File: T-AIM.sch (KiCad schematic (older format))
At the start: 30 parts, among them IC1 ATMEGA328PB-A

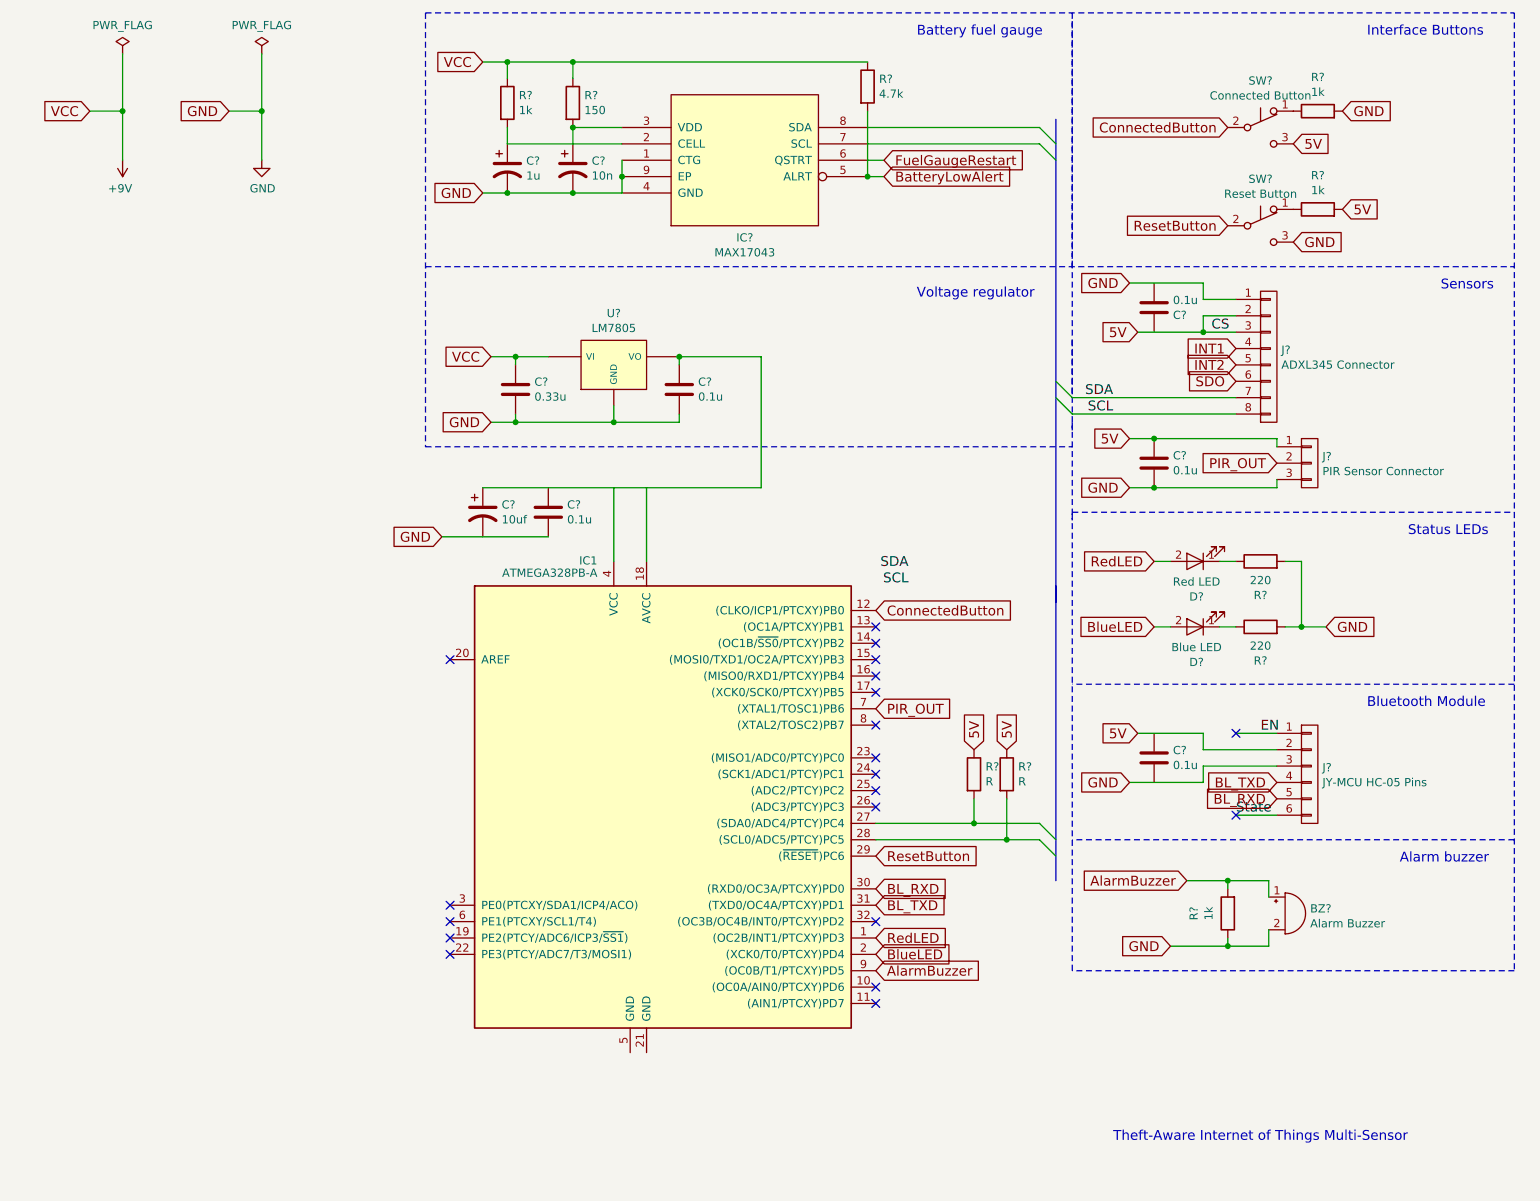
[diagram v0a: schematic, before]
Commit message: Schematic switches changed; PCB footprints assigned; Preliminary PCB layout set
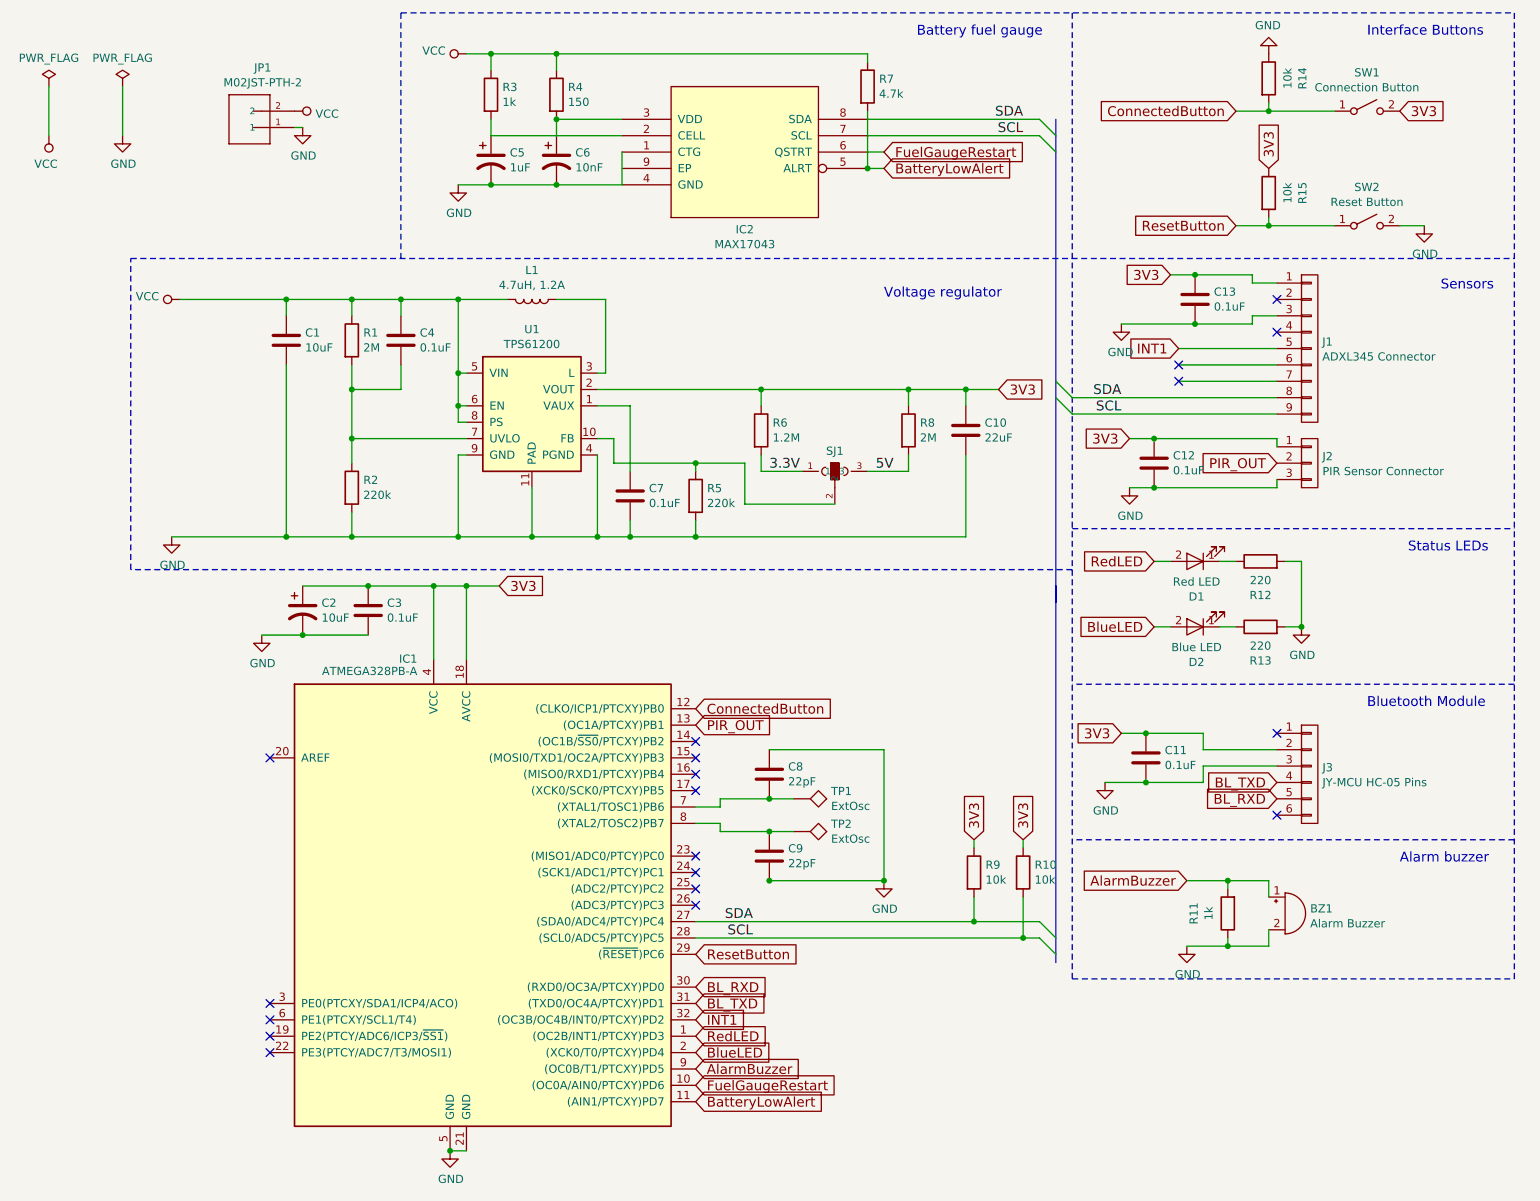
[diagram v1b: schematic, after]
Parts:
- removed BZ?: Alarm Buzzer, symbol Buzzer
- removed C? (x5): 0.1u, symbol C
- removed C?: 0.33u, symbol C
- removed C?: 1u, symbol CP1
- removed C?: 10n, symbol CP1
- removed C?: 10uf, symbol CP1
- removed D?: Red LED, symbol LED
- removed D?: Blue LED, symbol LED
- removed IC?: MAX17043, symbol MAX17043
- removed J?: ADXL345 Connector, symbol CONN_01X08
- removed J?: PIR Sensor Connector, symbol CONN_01X03
- removed J?: JY-MCU HC-05 Pins, symbol CONN_01X06
- removed R? (x2): 220, symbol R
- removed R? (x4): 1k, symbol R
- removed R? (x2): R, symbol R
- removed R?: 4.7k, symbol R
- removed R?: 150, symbol R
- removed SW?: Reset Button, symbol SW_Push_SPDT
- removed SW?: Connected Button, symbol SW_Push_SPDT
- removed U?: LM7805, symbol LM7805
- added BZ1: Alarm Buzzer, T-AIM:AT-1220-TT-9-R, symbol Buzzer
- added C1: 10uF, Capacitors_SMD:C_1812_HandSoldering, symbol C
- added C10: 22uF, Capacitors_SMD:C_1812_HandSoldering, symbol C
- added C11, C12, C13, C3, C4, C7: 0.1uF, Capacitors_SMD:C_1812_HandSoldering, symbol C
- added C2: 10uF, Capacitors_SMD:CP_Elec_5x5.3, symbol CP1
- added C5: 1uF, Capacitors_SMD:CP_Elec_5x5.3, symbol CP1
- added C6: 10nF, Capacitors_SMD:CP_Elec_5x5.3, symbol CP1
- added C8, C9: 22pF, Capacitors_SMD:C_1812_HandSoldering, symbol C
- added D1: Red LED, SparkFun-LED:LED-1206, symbol LED
- added D2: Blue LED, SparkFun-LED:LED-1206, symbol LED
- added IC2: MAX17043, SparkFun-PowerIC:TDFN-8, symbol MAX17043
- added J1: ADXL345 Connector, Pin_Headers:Pin_Header_Straight_1x09_Pitch2.54mm, symbol CONN_01X09
- added J2: PIR Sensor Connector, TO_SOT_Packages_THT:TO-5-3, symbol CONN_01X03
- added J3: JY-MCU HC-05 Pins, Pin_Headers:Pin_Header_Straight_1x06_Pitch2.54mm, symbol CONN_01X06
- added JP1: M02JST-PTH-2, SparkFun-Connectors:JST-2-PTH, symbol M02JST-PTH-2
- added L1: 4.7uH, 1.2A, SparkFun-Passives:INDUCTOR_4.7UH, symbol L
- added R1, R8: 2M, Resistors_SMD:R_0805_HandSoldering, symbol R
- added R10, R14, R15, R9: 10k, Resistors_SMD:R_0805_HandSoldering, symbol R
- added R11, R3: 1k, Resistors_SMD:R_0805_HandSoldering, symbol R
- added R12, R13: 220, Resistors_SMD:R_0805_HandSoldering, symbol R
- added R2, R5: 220k, Resistors_SMD:R_0805_HandSoldering, symbol R
- added R4: 150, Resistors_SMD:R_0805_HandSoldering, symbol R
- added R6: 1.2M, Resistors_SMD:R_0805_HandSoldering, symbol R
- added R7: 4.7k, Resistors_SMD:R_0805_HandSoldering, symbol R
- added SJ1: SOLDERJUMPER_2WAY-OLDPASTE1&2, SparkFun-Passives:SJ_3, symbol SOLDERJUMPER_2WAY-OLDPASTE1&2
- added SW1: Connection Button, Buttons_Switches_SMD:SW_SPST_PTS645, symbol SW_SPST
- added SW2: Reset Button, Buttons_Switches_SMD:SW_SPST_PTS645, symbol SW_SPST
- added TP1, TP2: ExtOsc, Connectors:PINTST, symbol TEST
- added U1: TPS61200, SparkFun-PowerIC:DRC-10, symbol TPS61200
- IC1: footprint Housings_QFP:LQFP-32_5x5mm_Pitch0.5mm -> Housings_QFP:TQFP-32_7x7mm_Pitch0.8mm
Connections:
- net 5V: now also R8.2, SJ1.3
- net AlarmBuzzer: now also BZ1.1 (-), R11.2
- net BL_RXD: now also J3.5 (P5)
- net BL_TXD: now also J3.4 (P4)
- net BatteryLowAlert: now also IC1.11 ((AIN1/PTCXY)PD7), IC2.5 (ALRT), R7.2
- net BlueLED: now also D2.2 (A)
- net ConnectedButton: now also R14.2, SW1.1 (A)
- net FuelGaugeRestart: now also IC1.10 ((OC0A/AIN0/PTCXY)PD6), IC2.6 (QSTRT)
- net GND: now also IC1.21 (GND), IC1.5 (GND), BZ1.2 (+), C1.2, C10.2, C11.2, C12.2, C13.2, C2.2, C3.2, C5.2, C6.2, C7.2, C8.1, C9.2, IC2.1 (CTG), IC2.4 (GND), IC2.9 (EP), J1.3 (P3), J2.3 (P3), J3.3 (P3), JP1.1, R11.1, R12.2, R13.2, R14.1, R2.2, R5.2, SW2.2 (B), U1.11 (PAD), U1.4 (PGND), U1.9 (GND)
- net INT1: now also IC1.32 ((OC3B/OC4B/INT0/PTCXY)PD2), J1.5 (P5)
- net PIR_OUT: now also IC1.13 ((OC1A/PTCXY)PB1), J2.2 (P2); no longer IC1.7 ((XTAL1/TOSC1)PB6)
- net RedLED: now also D1.2 (A)
- net ResetButton: now also R15.2, SW2.1 (A)
- net SCL: now also IC1.28 ((SCL0/ADC5/PTCY)PC5), IC2.7 (SCL), J1.9 (P9), R10.2
- net SDA: now also IC1.27 ((SDA0/ADC4/PTCY)PC4), IC2.8 (SDA), J1.8 (P8), R9.2
- net 3V3: now reaches IC1.18 (AVCC)
- net 3V3: now also IC1.4 (VCC), C10.1, C11.1, C12.1, C13.1, C2.1, C3.1, J1.1 (P1), J2.1 (P1), J3.2 (P2), R10.1, R15.1, R6.1, R8.1, R9.1, SW1.2 (B), U1.2 (VOUT)
- net at IC1.8 ((XTAL2/TOSC2)PB7): now also C9.1, TP2.1
- new net: D1.1 (K), R12.1
- new net: D2.1 (K), R13.1
- new net: C5.1, IC2.2 (CELL), R3.2
- new net: C6.1, IC2.3 (VDD), R4.2
- new net: C8.2, IC1.7 ((XTAL1/TOSC1)PB6), TP1.1
- new net: C7.1, U1.1 (VAUX)
- new net: R5.1, SJ1.2, U1.10 (FB)
- new net: L1.1, U1.3 (L)
- new net: C4.2, R1.2, R2.1, U1.7 (UVLO)
- new net 3.3V: R6.2, SJ1.1
- new net VCC: C1.1, C4.1, JP1.2, L1.2, R1.1, R3.1, R4.1, R7.1, U1.5 (VIN), U1.6 (EN), U1.8 (PS)
- no-connect marks 20 -> 19
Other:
- note removed: "Theft-Aware Internet of Things Multi-Sensor"

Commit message: Layout started
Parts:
- D1, D2: footprint SparkFun-LED:LED-1206 -> LEDs:LED_1206
- L1: footprint SparkFun-Passives:INDUCTOR_4.7UH -> T-AIM:INDUCTOR_4.7UH
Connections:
- net AlarmBuzzer: now also IC1.24 ((SCK1/ADC1/PTCY)PC1); no longer IC1.9 ((OC0B/T1/PTCXY)PD5)
- net BatteryLowAlert: now also IC1.26 ((ADC3/PTCY)PC3); no longer IC1.11 ((AIN1/PTCXY)PD7)
- net BlueLED: now also IC1.1 ((OC2B/INT1/PTCXY)PD3); no longer IC1.2 ((XCK0/T0/PTCXY)PD4)
- net ConnectedButton: now also IC1.19 (PE2(PTCY/ADC6/ICP3/~SS1~)); no longer IC1.12 ((CLKO/ICP1/PTCXY)PB0)
- net FuelGaugeRestart: now also IC1.25 ((ADC2/PTCY)PC2); no longer IC1.10 ((OC0A/AIN0/PTCXY)PD6)
- net RedLED: now also IC1.2 ((XCK0/T0/PTCXY)PD4); no longer IC1.1 ((OC2B/INT1/PTCXY)PD3)
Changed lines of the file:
@@
 NoConn ~ 4850 5150
 NoConn ~ 4850 5250
-NoConn ~ 4850 5850
-NoConn ~ 4850 5950
-NoConn ~ 4850 6050
 NoConn ~ 2250 6950
-NoConn ~ 2250 6850
 NoConn ~ 2250 5150
 NoConn ~ 4850 5750
@@
 F 0 "D1" H 7891 4166 50  0000 C CNN
 F 1 "Red LED" H 7891 4075 50  0000 C CNN
-F 2 "SparkFun-LED:LED-1206" H 3550 -750 50  0001 C CNN
+F 2 "LEDs:LED_1206" H 3550 -750 50  0001 C CNN
 F 3 "http://optoelectronics.liteon.com/upload/download/DS-22-98-0002/S_110_LTST-C150CKT.pdf" H 3550 -750 50  0001 C CNN
 	1    7900 3950
@@
 F 0 "D2" H 7891 4566 50  0000 C CNN
 F 1 "Blue LED" H 7891 4475 50  0000 C CNN
-F 2 "SparkFun-LED:LED-1206" H 3550 -350 50  0001 C CNN
+F 2 "LEDs:LED_1206" H 3550 -350 50  0001 C CNN
 F 3 "http://optoelectronics.liteon.com/upload/download/DS22-2000-026/S_110_LTST-C150TBKT(0630).pdf" H 3550 -350 50  0001 C CNN
 	1    7900 4350
 	-1   0    0    1
 $EndComp
+Text GLabel 4850 6950 2    60   Input ~ 0
+RedLED
 Text GLabel 4850 6850 2    60   Input ~ 0
-RedLED
-Text GLabel 4850 6950 2    60   Input ~ 0
 BlueLED
 $Comp
@@
 Text GLabel 7650 4350 0    60   Input ~ 0
 BlueLED
-Text GLabel 4850 7050 2    60   Input ~ 0
+Text GLabel 4850 5850 2    60   Input ~ 0
 AlarmBuzzer
 Text GLabel 7850 5900 0    60   Input ~ 0
@@
 Text GLabel 4850 6350 2    60   Input ~ 0
 ResetButton
-Text GLabel 4850 4850 2    60   Input ~ 0
+Text GLabel 2250 6850 0    60   Input ~ 0
 ConnectedButton
 Text GLabel 4850 4950 2    60   Input ~ 0
@@
 F 0 "L1" V 3672 2350 50  0000 C CNN
 F 1 "4.7uH, 1.2A" V 3763 2350 50  0000 C CNN
-F 2 "SparkFun-Passives:INDUCTOR_4.7UH" H -10500 -1400 50  0001 C CNN
+F 2 "T-AIM:INDUCTOR_4.7UH" H -10500 -1400 50  0001 C CNN
 F 3 "http://products.sumida.com/products/pdf/CDRH2D09.pdf" H -10500 -1400 50  0001 C CNN
 	1    3850 2350
@@
 	-1   0    0    1
 $EndComp
-Text GLabel 4850 7150 2    60   Input ~ 0
+Text GLabel 4850 5950 2    60   Input ~ 0
 FuelGaugeRestart
-Text GLabel 4850 7250 2    60   Input ~ 0
+Text GLabel 4850 6050 2    60   Input ~ 0
 BatteryLowAlert
 $Comp
@@
 Wire Wire Line
 	9300 1900 9150 1900
+NoConn ~ 4850 7150
+NoConn ~ 4850 7250
+NoConn ~ 4850 7050
+NoConn ~ 4850 4850
 $EndSCHEMATC
